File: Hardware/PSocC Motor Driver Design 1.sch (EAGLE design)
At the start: 41 parts

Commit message: Sending it home
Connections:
- new net P2.3: U$1G$3.P2.3, U$2.MODE
- net P2.0: no longer U$2.MODE
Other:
- note added: "0000: UART 0001: SPI 0010: Slave device (User port unused) 0011: I2C addr 0x58 0100: I2C addr 0x59 0101: I2C addr 0x5A 0110: I2C addr 0x5B (...) 1100: I2C addr 0x61 1101: I2C addr 0x62 1110: I2C addr 0x63 1111: RC-style PWM"
- note added: "1.1"
- note added: "3.3V Regulator"
- note added: "A driver for controlling 2 (or more) DC motors."
- note added: "Config Jumpers"
- note added: "H-Bridge Driver"
- note added: "Marshall Taylor"
- note added: "PSoC I/O"
- note added: "PSoC Power and Filtering"
- note added: "Power Port"
- note added: "Programming Header"
- note added: "Serial Controlled Motor Driver"
- note added: "Serial Ports"
- note removed: "Title block"
- moved on the sheet: J5, J6, JP5, R4, R5

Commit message: Working on checklist
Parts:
- JP1, JP2, JP3, JP4: value JUMPER-PAD-2-NOYES_SILK -> JUMPER-PAD-2
- renumbered U$1 to U1, U$2 to U2
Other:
- note added: "1.5"
- note added: "The default, all open, is the UART mode. A '1' indicated solder bridge."
- note removed: "1.1"

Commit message: Finished checklist
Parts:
- added D1: RED, SparkFun-LED:LED-RED0603
- added R6: 470, SparkFun-Resistors:470OHM-0603-1/10W-1%
- J1, J2, J3, J4, J5, J6, J7: value (none) -> DNP
- R3, R4, R5: value 1 -> 4.7k; device SparkFun-Resistors:1OHM-0603-1/10W-1% -> SparkFun-Resistors:4.7KOHM-0603-1/10W-1%
- U1: device SparkFun-DigitalIC:CY8C4245LQI -> PSOC4TempLib:CY8C4245LQI
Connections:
- new net N$10: D1.A, R6.2
- net !RESET: now also U1G6.XRES; no longer U1G$6.XRES
- net CLK_IN: now also U1G1.P0.6; no longer U1G$1.P0.6
- net CONFIG_IN: now also U1G4.P3.0; no longer U1G$4.P3.0
- net CONFIG_OUT: now also U1G4.P3.1; no longer U1G$4.P3.1
- net GND: now also D1.C, U1G6.VSS, U1G6.VSSA; no longer U1G$6.VSS, U1G$6.VSSA
- net MODEB0: now also U1G1.P0.0; no longer U1G$1.P0.0
- net MODEB1: now also U1G1.P0.1; no longer U1G$1.P0.1
- net MODEB2: now also U1G1.P0.2; no longer U1G$1.P0.2
- net MODEB3: now also U1G1.P0.3; no longer U1G$1.P0.3
- net N$1: now also U1G6.VCCD; no longer U1G$6.VCCD
- net N$3: now also U1G6.VDDA; no longer U1G$6.VDDA
- net N$4: now also U1G6.VREF; no longer U1G$6.VREF
- net P2.0: now also R6.1, U1G3.P2.0; no longer U1G$3.P2.0
- net P2.3: now also U1G3.P2.3; no longer U1G$3.P2.3
- net P2.4: now also U1G3.P2.4; no longer U1G$3.P2.4
- net P2.5: now also U1G3.P2.5; no longer U1G$3.P2.5
- net P2.6: now also U1G3.P2.6; no longer U1G$3.P2.6
- net P2.7: now also U1G3.P2.7; no longer U1G$3.P2.7
- net P3.4_US: now also U1G4.P3.4; no longer U1G$4.P3.4
- net P3.5_US: now also U1G4.P3.5; no longer U1G$4.P3.5
- net P3.6: now also U1G4.P3.6; no longer U1G$4.P3.6
- net P3.7: now also U1G4.P3.7; no longer U1G$4.P3.7
- net RX_SCL_MOSI_IN: now also U1G1.P0.4; no longer U1G$1.P0.4
- net SCL_OUT: now also U1G5.P4.0; no longer U1G$5.P4.0
- net SDA_OUT: now also U1G5.P4.1; no longer U1G$5.P4.1
- net SS_IN: now also U1G1.P0.7; no longer U1G$1.P0.7
- net TEST1: now also U1G4.P3.2; no longer U1G$4.P3.2
- net TEST2: now also U1G4.P3.3; no longer U1G$4.P3.3
- net TX_SDA_MISO_IN: now also U1G1.P0.5; no longer U1G$1.P0.5
- net VDDD: now also U1G6.VDDD; no longer U1G$6.VDDD
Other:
- note added: "Status"

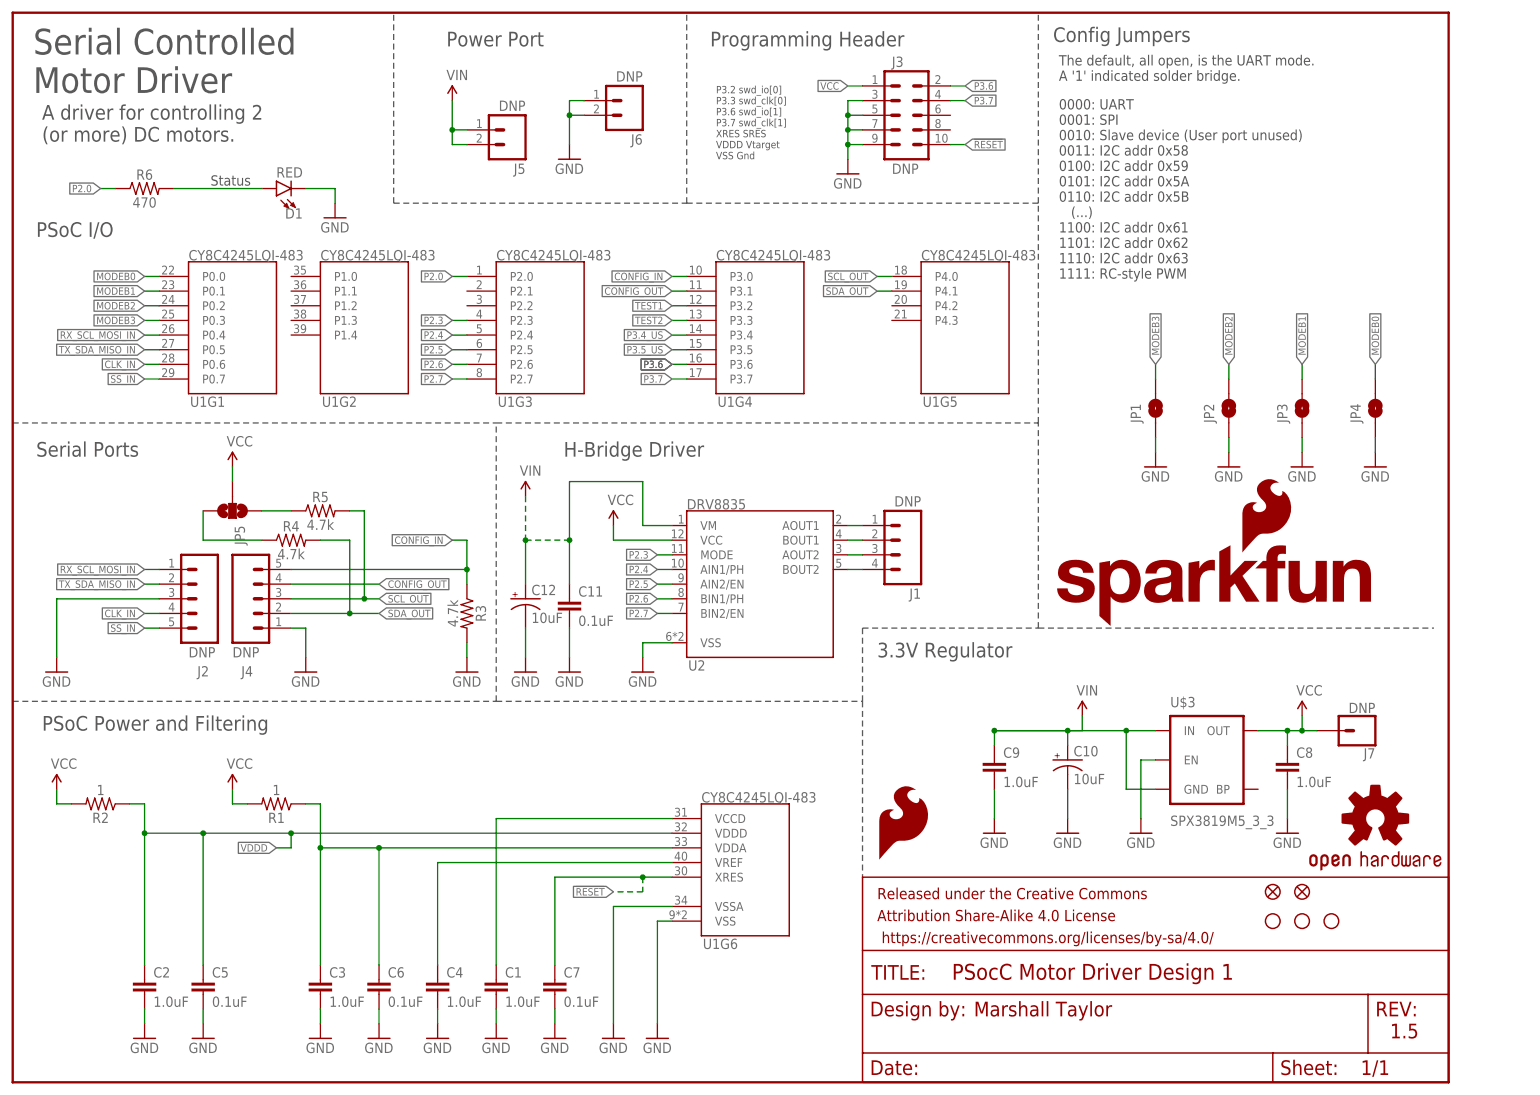
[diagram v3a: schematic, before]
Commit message: bringing branch up to date with physical hardware v1.5
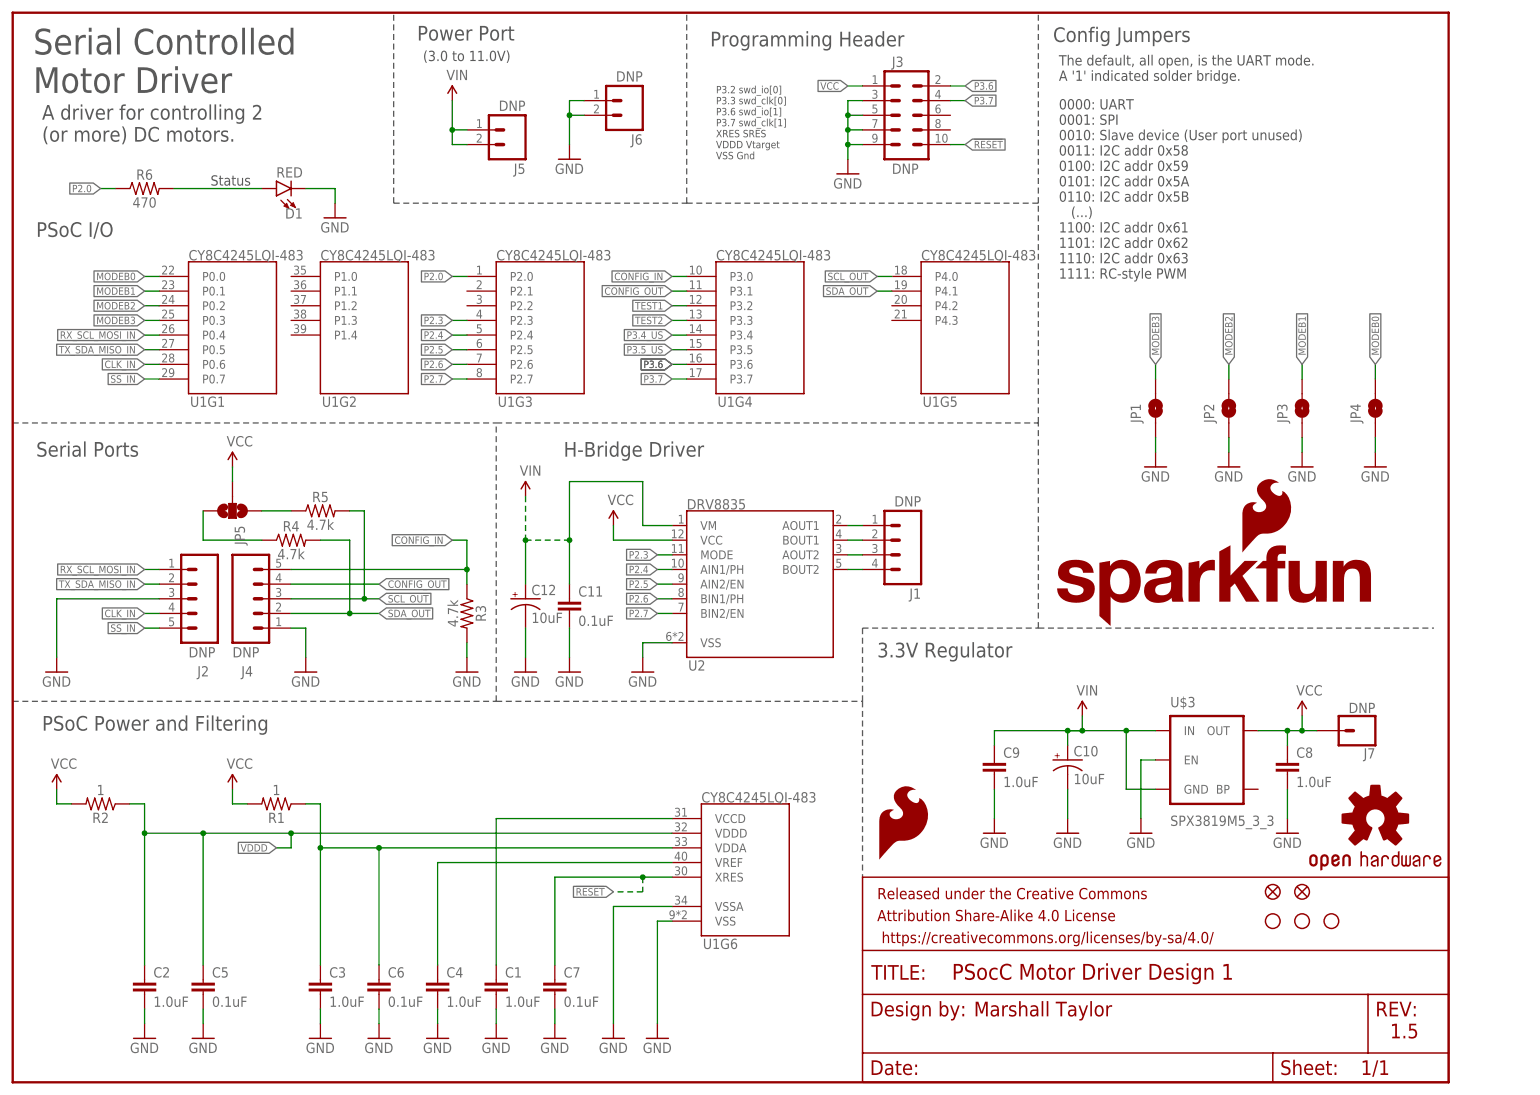
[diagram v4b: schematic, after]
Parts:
- U2: PROD_ID (none) -> IC-13342
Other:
- note added: "(3.0 to 11.0V)"
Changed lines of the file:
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@@
 <part name="C7" library="SparkFun-Capacitors" deviceset="0.1UF" device="-0402-16V-10%" value="0.1uF"/>
 <part name="GND9" library="SparkFun-Aesthetics" deviceset="GND" device=""/>
-<part name="U2" library="PSOC4TempLib" deviceset="DRV883X" device="" value="DRV8835"/>
+<part name="U2" library="PSOC4TempLib" deviceset="DRV883X" device="" value="DRV8835">
+<attribute name="PROD_ID" value="IC-13342"/>
+</part>
 <part name="J1" library="SparkFun-Connectors" deviceset="M04" device="PTH" value="DNP"/>
 <part name="GND10" library="SparkFun-Aesthetics" deviceset="GND" device=""/>
@@
 VSS Gnd</text>
 <text x="4.064" y="108.458" size="2.54" layer="97" font="vector" ratio="15">Serial Ports</text>
-<text x="75.184" y="179.578" size="2.54" layer="97" font="vector" ratio="15">Power Port</text>
+<text x="70.104" y="180.594" size="2.54" layer="97" font="vector" ratio="15">Power Port</text>
 <text x="120.904" y="179.578" size="2.54" layer="97" font="vector" ratio="15">Programming Header</text>
 <text x="95.504" y="108.458" size="2.54" layer="97" font="vector" ratio="15">H-Bridge Driver</text>
@@
 A '1' indicated solder bridge.</text>
 <text x="34.29" y="157.226" size="1.778" layer="97" font="vector" align="top-left">Status</text>
+<text x="71.12" y="177.038" size="1.778" layer="97" font="vector" ratio="15">(3.0 to 11.0V)</text>
 </plain>
 <instances>
@@
 <wire x1="193.04" y1="50.8" x2="193.04" y2="60.96" width="0.1524" layer="91"/>
 <junction x="193.04" y="60.96"/>
-<wire x1="193.04" y1="60.96" x2="182.88" y2="60.96" width="0.1524" layer="91"/>
+<wire x1="193.04" y1="60.96" x2="185.42" y2="60.96" width="0.1524" layer="91"/>
+<wire x1="185.42" y1="60.96" x2="182.88" y2="60.96" width="0.1524" layer="91"/>
 <wire x1="182.88" y1="60.96" x2="170.18" y2="60.96" width="0.1524" layer="91"/>
-<wire x1="170.18" y1="60.96" x2="185.42" y2="60.96" width="0.1524" layer="91"/>
+<wire x1="182.88" y1="60.96" x2="185.42" y2="60.96" width="0.1524" layer="91"/>
 <wire x1="185.42" y1="60.96" x2="185.42" y2="63.5" width="0.1524" layer="91"/>
 <pinref part="SUPPLY10" gate="G$1" pin="VIN"/>
 <pinref part="C9" gate="G$1" pin="1"/>
 <wire x1="170.18" y1="58.42" x2="170.18" y2="60.96" width="0.1524" layer="91"/>
-<junction x="170.18" y="60.96"/>
 <pinref part="U$3" gate="G$1" pin="IN"/>
 <pinref part="U$3" gate="G$1" pin="GND"/>
@@
 <wire x1="182.88" y1="60.96" x2="182.88" y2="58.42" width="0.1524" layer="91"/>
 <junction x="182.88" y="60.96"/>
-</segment>
-<segment>
+<junction x="185.42" y="60.96"/>
+</segment>
+<segment>
